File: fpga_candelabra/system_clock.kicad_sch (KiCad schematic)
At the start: 37 parts, among them U22 CDCM6208V1, Y2 NX3225GA 25MHz

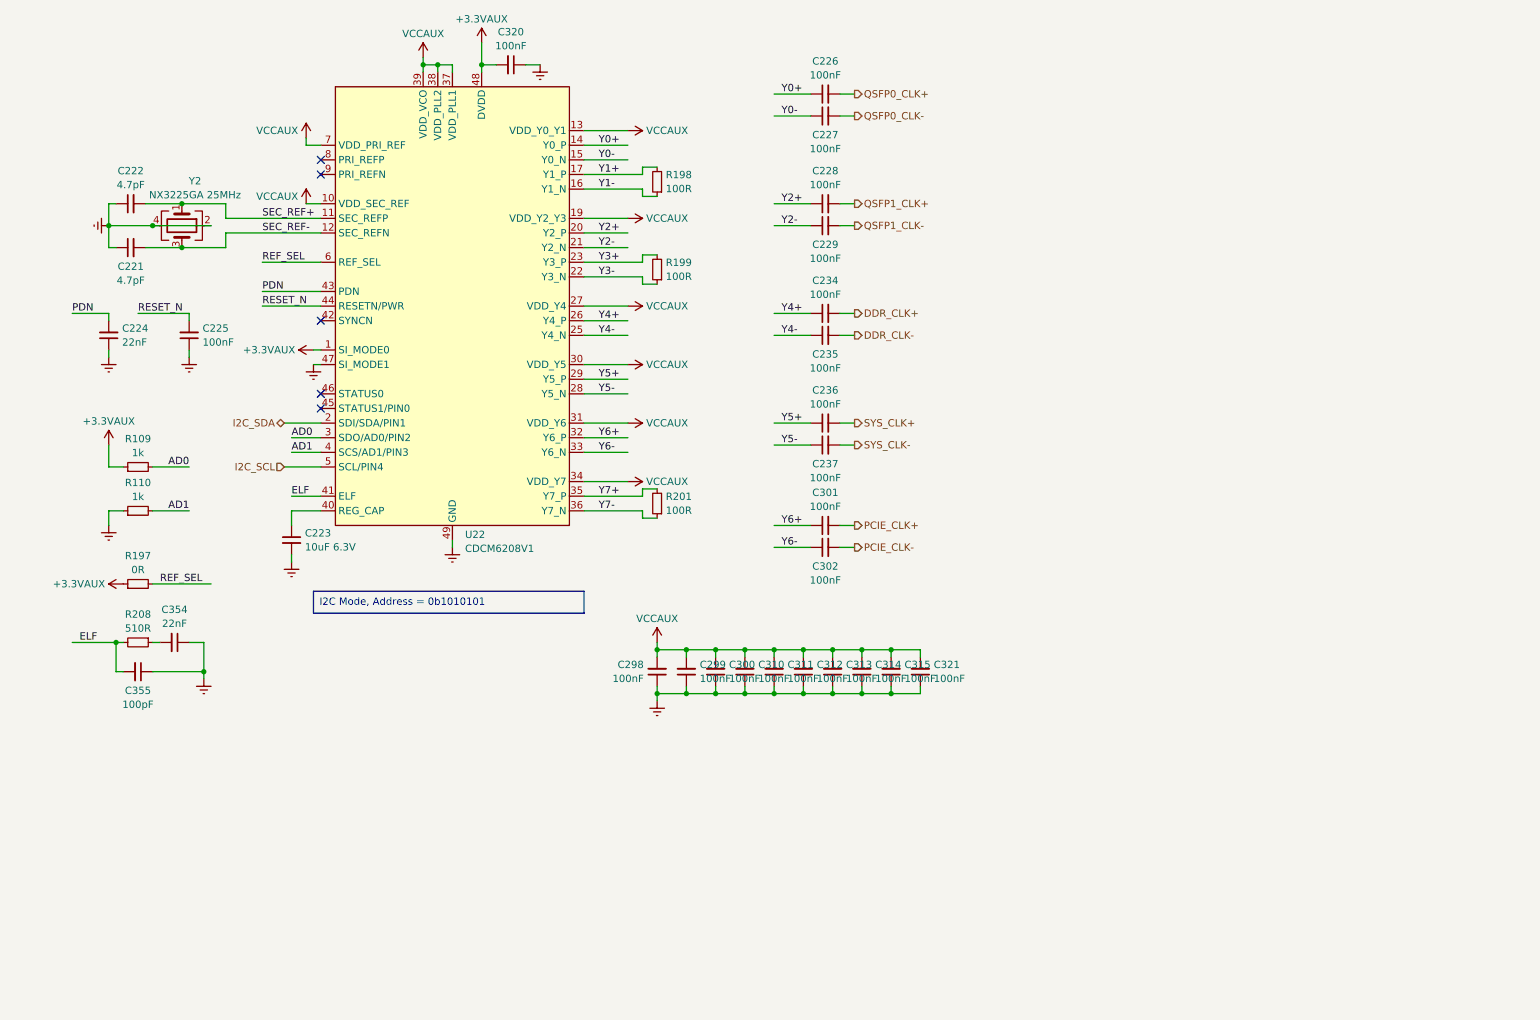
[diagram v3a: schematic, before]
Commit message: fpga_candelabra: more bugfixes & improvements for rev 0.2.0
- Add Digilent JTAG-SMT2-NC onboard
- Add fan controller & 4pin fan header
- Use 9pin header for USB2.0
- Misc fixes for structure

Signed-off-by: Yichuan Gao <gaoyichuan000@gmail.com>
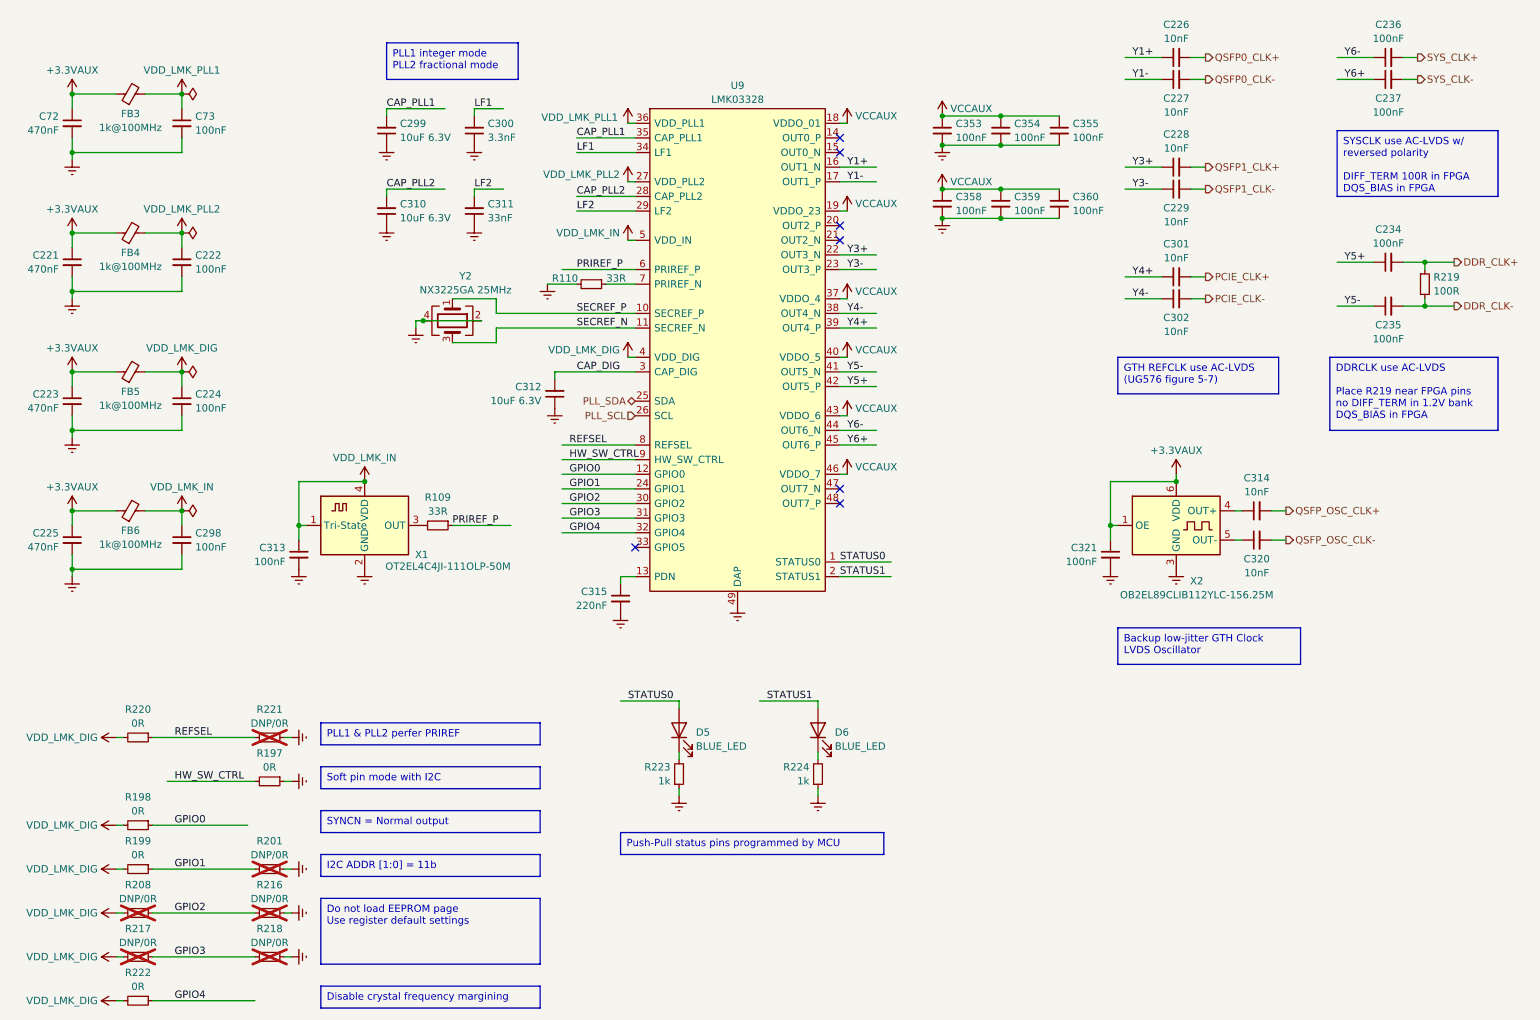
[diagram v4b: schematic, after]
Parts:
- removed U22: CDCM6208V1, Package_DFN_QFN:Texas_RGZ0048A_VQFN-48-1EP_7x7mm_P0.5mm_EP5.15x5.15mm_ThermalVias, symbol CHIPSAlliance_Timer_PLL:CDCM6208V1
- added C353, C358, C359, C360, C73: 100nF, Capacitor_SMD:C_0402_1005Metric, symbol Device:C_Small
- added C72: 470nF, Capacitor_SMD:C_0402_1005Metric, symbol Device:C_Small
- added D5, D6: BLUE_LED, LED_SMD:LED_0603_1608Metric, symbol Device:LED
- added FB3, FB4, FB5, FB6: 1k@100MHz, Inductor_SMD:L_0402_1005Metric, symbol Device:FerriteBead_Small
- added R216, R217, R218, R221: DNP/0R, Resistor_SMD:R_0402_1005Metric, symbol Device:R_Small
- added R219: 100R, Resistor_SMD:R_0402_1005Metric, symbol Device:R_Small
- added R220, R222: 0R, Resistor_SMD:R_0402_1005Metric, symbol Device:R_Small
- added R223, R224: 1k, Resistor_SMD:R_0402_1005Metric, symbol Device:R_Small
- added U9: LMK03328, CHIPSAlliance_Package_DFN_QFN:Texas_RHS0048B_WQFN-48-1EP_7x7mm_P0.5mm_EP5.2x5.2mm_ThermalVias, symbol CHIPSAlliance_Timer_PLL:LMK03328
- added X1: OT2EL4C4JI-111OLP-50M, Oscillator:Oscillator_SMD_Abracon_ASE-4Pin_3.2x2.5mm, symbol Oscillator:ASCO
- added X2: OB2EL89CLIB112YLC-156.25M, CHIPSAlliance_Oscillator:Oscillator_SMD_YXC_YSO230LR-6Pin_3.2x2.5mm, symbol Oscillator:SiT9365xx-xBx-xxE
- C221: value 4.7pF -> 470nF
- C222: value 4.7pF -> 100nF
- C223: value 10uF 6.3V -> 470nF
- C224, C354: value 22nF -> 100nF
- C225: value 100nF -> 470nF
- C226, C227, C228, C229, C301, C302, C314, C320: value 100nF -> 10nF
- C299, C310, C312: value 100nF -> 10uF 6.3V
- C300: value 100nF -> 3.3nF
- C311: value 100nF -> 33nF
- C315: value 100nF -> 220nF
- C355: value 100pF -> 100nF
- R109, R110: value 1k -> 33R
- R198, R199: value 100R -> 0R
- R201: value 100R -> DNP/0R; now not fitted
- R208: value 510R -> DNP/0R; now not fitted
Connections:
- net AD1 is gone; now on net Earth: R110.2
- net PDN is gone; now on net Earth: C224.2
- net RESET_N is gone; now on net Earth: C225.2
- net Y0+ is gone; now on net Y1+: C226.1
- net Y0- is gone; now on net Y1-: C227.1
- net Y2+ is gone; now on net Y3+: C228.1
- net Y2- is gone; now on net Y3-: C229.1
- net Y7- is gone; now on net Earth: R201.1
- net +3.3VAUX: now also C221.1, C223.1, C225.1, C321.1, C72.1, FB3.1, FB4.1, FB5.1, FB6.1, X2.1 (OE), X2.6 (VDD); no longer C320.2, R109.1, R197.1
- net DDR_CLK+: now also R219.1
- net DDR_CLK-: now also R219.2
- net Earth: now also C221.2, C222.2, C298.2, C313.2, C315.2, C321.2, C354.2, C355.2, R197.1, C353.2, C358.2, C359.2, C360.2, C72.2, C73.2, R216.1, R218.1, R221.1, R223.1, R224.1, U9.49 (DAP), X1.2 (GND), X2.3 (GND); no longer C221.1, C222.1, C224.1, C225.1, C298.1, C313.1, C314.1, C315.1, C320.1, C321.1, C354.1, C355.1, R110.1
- net VCCAUX: now also C354.1, C355.1, C353.1, C358.1, C359.1, C360.1, U9.18 (VDDO_01), U9.19 (VDDO_23), U9.37 (VDDO_4), U9.40 (VDDO_5), U9.43 (VDDO_6), U9.46 (VDDO_7); no longer C298.2, C299.2, C300.2, C310.2, C311.2, C312.2, C313.2, C314.2, C315.2, C321.2
- net Y1+: now also U9.16 (OUT1_N); no longer R198.2
- net Y1-: now also U9.17 (OUT1_P); no longer R198.1
- net Y3+: now also U9.22 (OUT3_N); no longer R199.2
- net Y3-: now also U9.23 (OUT3_P); no longer R199.1
- net Y4+: now also C301.1, U9.39 (OUT4_P); no longer C234.1
- net Y4-: now also C302.1, U9.38 (OUT4_N); no longer C235.1
- net Y5+: now also C234.1, U9.42 (OUT5_P); no longer C236.1
- net Y5-: now also C235.1, U9.41 (OUT5_N); no longer C237.1
- net Y6+: now also C237.1, U9.45 (OUT6_P); no longer C301.1
- net Y6-: now also C236.1, U9.44 (OUT6_N); no longer C302.1
- net GPIO2: now reaches R208.1
- net GPIO2: now also R216.2, U9.30 (GPIO2); no longer C354.2
- net AD0: no longer names the net of R109.2
- net AD0: now also X1.3 (OUT)
- net ELF renamed VDD_LMK_DIG
- net VDD_LMK_DIG: now also C224.1, R198.2, R199.2, FB5.2, R217.2, R220.2, R222.2, U9.4 (VDD_DIG); no longer C355.2
- net REF_SEL renamed HW_SW_CTRL
- net HW_SW_CTRL: now also U9.9 (HW_SW_CTRL)
- net SEC_REF+ renamed SECREF_P
- net SECREF_P: now also U9.10 (SECREF_P); no longer C222.2
- net SEC_REF- renamed SECREF_N
- net SECREF_N: now also U9.11 (SECREF_N); no longer C221.2
- net Y7+ renamed GPIO1
- net GPIO1: now also R199.1, U9.24 (GPIO1)
- new net: D5.1 (K), R223.2
- new net: C314.1, X2.4 (OUT+)
- new net: D6.1 (K), R224.2
- new net: C320.1, X2.5 (OUT-)
- new net: C315.1, U9.13 (PDN)
- new net: R110.1, U9.7 (PRIREF_N)
- new net CAP_DIG: C312.2, U9.3 (CAP_DIG)
- new net CAP_PLL1: C299.2, U9.35 (CAP_PLL1)
- new net CAP_PLL2: C310.2, U9.28 (CAP_PLL2)
- new net GPIO0: R198.1, U9.12 (GPIO0)
- new net GPIO3: R217.1, R218.2, U9.31 (GPIO3)
- new net GPIO4: R222.1, U9.32 (GPIO4)
- new net LF1: C300.2, U9.34 (LF1)
- new net LF2: C311.2, U9.29 (LF2)
- new net PLL_SCL: U9.26 (SCL)
- new net PLL_SDA: U9.25 (SDA)
- new net PRIREF_P: R109.1, U9.6 (PRIREF_P)
- new net QSFP_OSC_CLK+: C314.2
- new net QSFP_OSC_CLK-: C320.2
- new net REFSEL: R220.1, R221.2, U9.8 (REFSEL)
- new net STATUS0: D5.2 (A), U9.1 (STATUS0)
- new net STATUS1: D6.2 (A), U9.2 (STATUS1)
- new net VDD_LMK_IN: C298.1, C313.1, FB6.2, U9.5 (VDD_IN), X1.1 (Tri-State), X1.4 (VDD)
- new net VDD_LMK_PLL1: C73.1, FB3.2, U9.36 (VDD_PLL1)
- new net VDD_LMK_PLL2: C222.1, FB4.2, U9.27 (VDD_PLL2)
- no-connect marks 5 -> 7
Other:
- moved on the sheet: C226, C227, C228, C229, C234, C235, C236, C237, C301, C302

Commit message: fpga_candelabra: add author & rev to schematics
Signed-off-by: Yichuan Gao <gaoyichuan000@gmail.com>
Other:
- company: (none) -> CHIPS Alliance
- title: (none) -> System PLL
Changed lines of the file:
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@@
 	(generator_version "8.0")
 	(paper "A4")
+	(title_block
+		(title "System PLL")
+		(date "2025-02-05")
+		(rev "0.2.0")
+		(company "CHIPS Alliance")
+		(comment 1 "Yichuan Gao")
+		(comment 2 "Yichuan Gao")
+	)
 	(junction
 		(at 46.99 54.61)

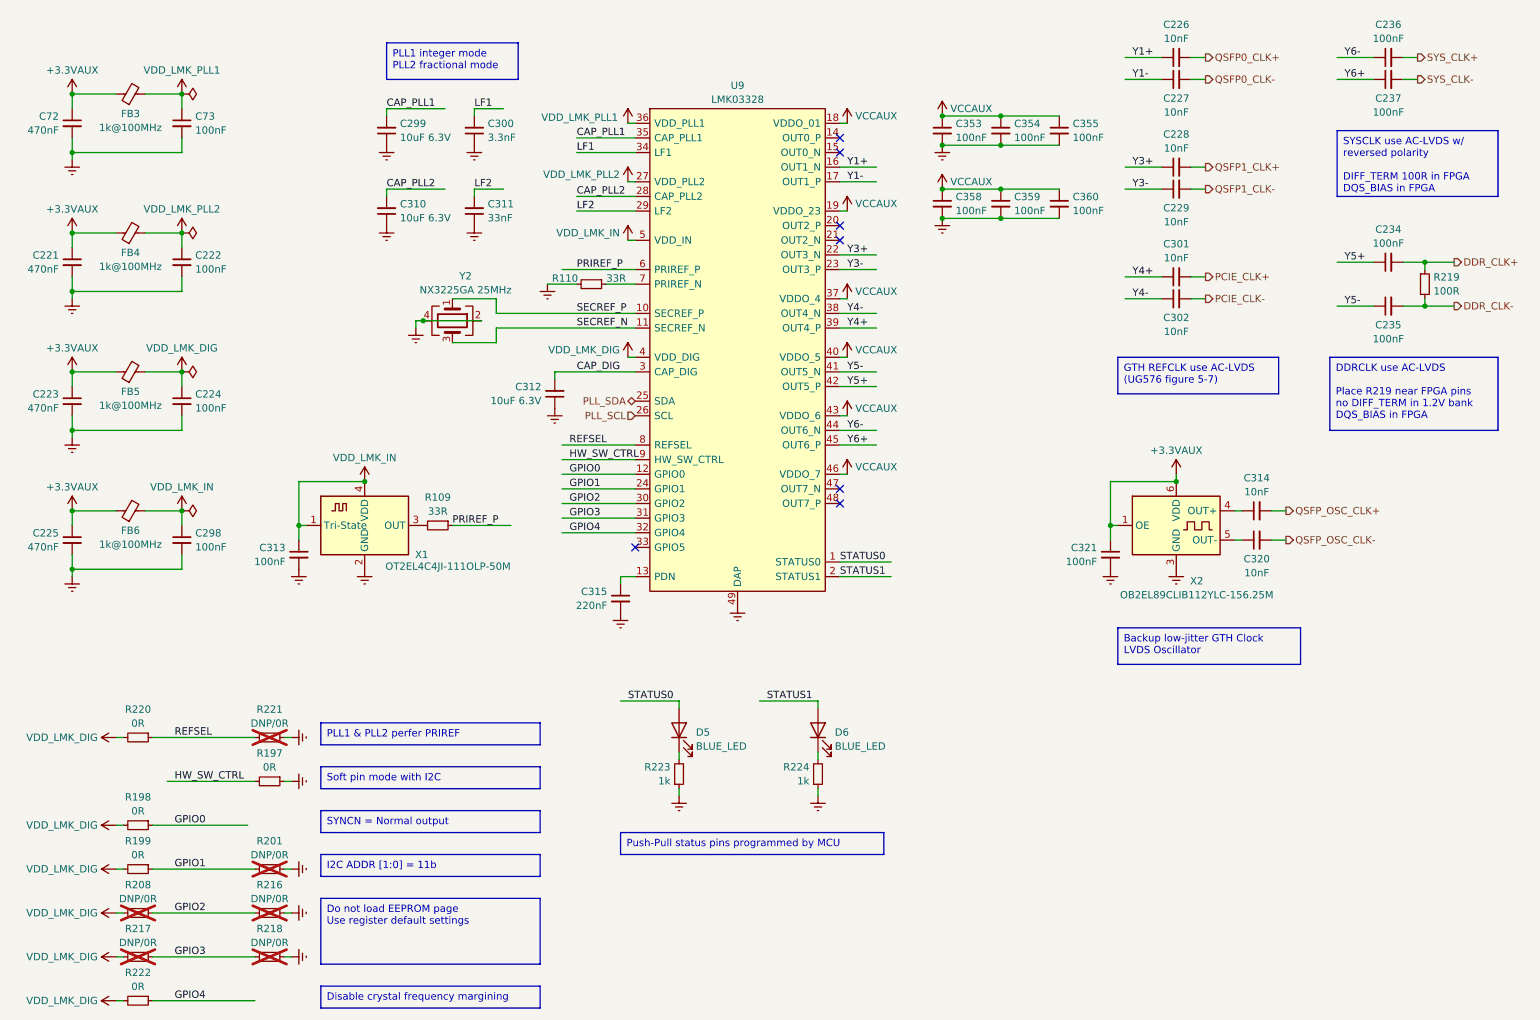
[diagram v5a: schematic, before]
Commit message: fpga_candelabra: update to kicad 9.0
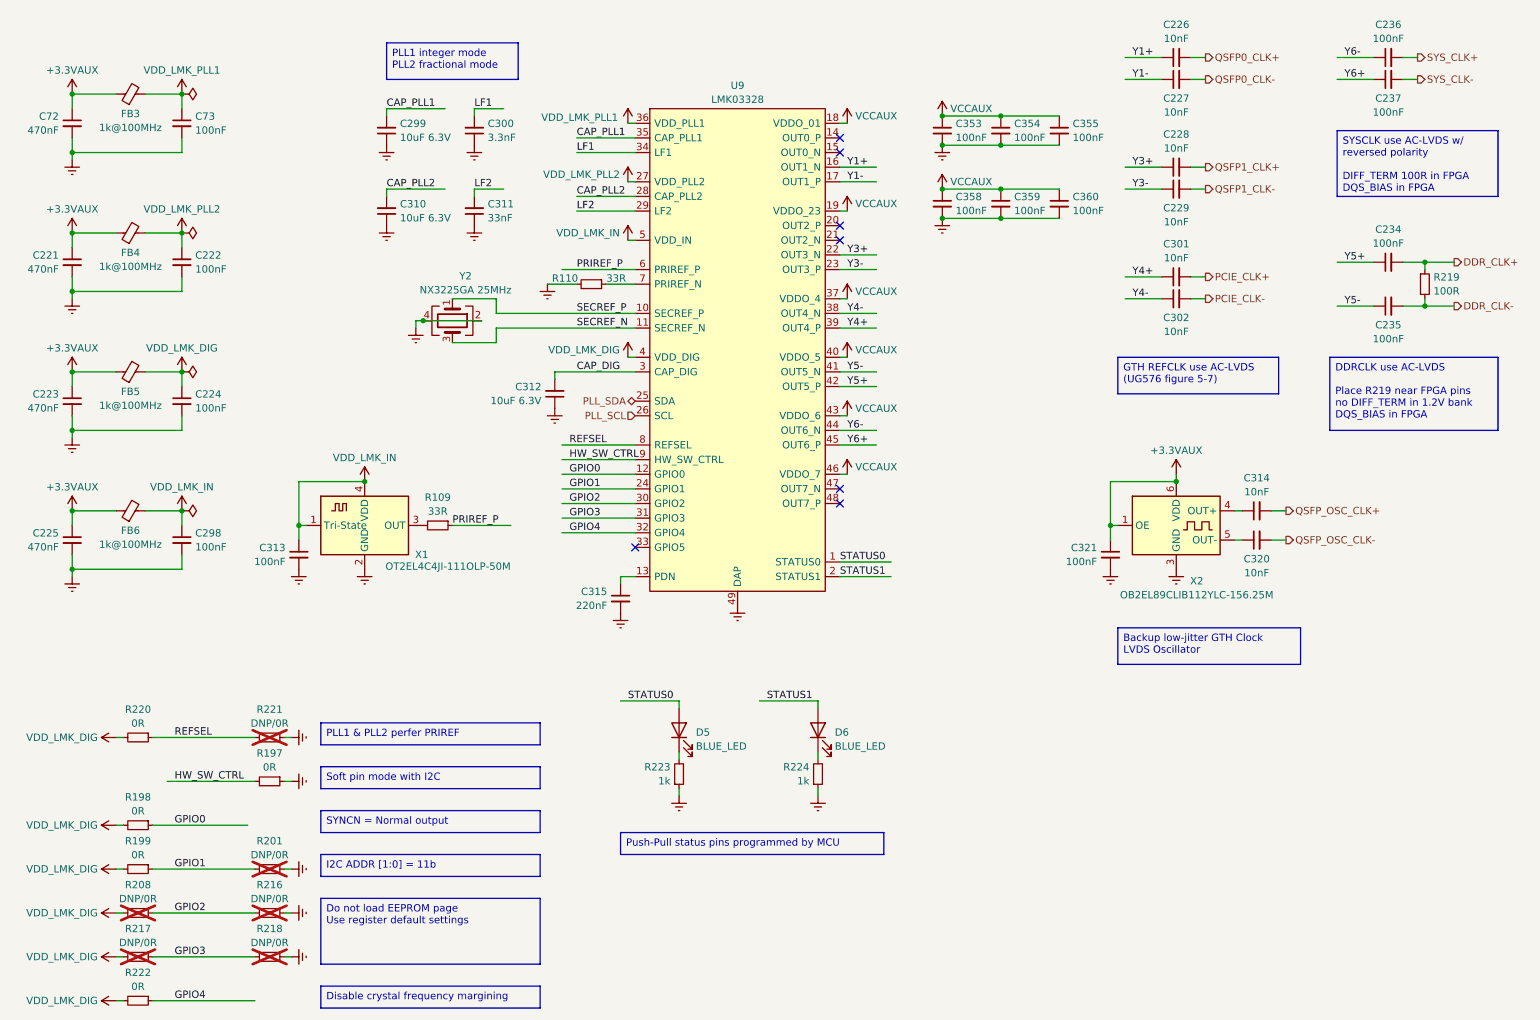
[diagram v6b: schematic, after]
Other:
- company: CHIPS Alliance -> Sipeed

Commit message: fpga_candelabra: update to kicad 10 and fix some 3d model path
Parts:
- X1: footprint Oscillator:Oscillator_SMD_Abracon_ASE-4Pin_3.2x2.5mm -> CHIPSAlliance_Oscillator:Oscillator_SMD_Abracon_ASE-4Pin_3.2x2.5mm
